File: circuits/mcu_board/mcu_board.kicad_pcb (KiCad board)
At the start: 2 copper layers, 96.3 x 63.9 mm, 44 parts, among them J1 USB_B_Micro, J2 Conn_01x13_Pin, J3 Conn_01x03_Pin, SW1 SW_Push, SW10 SW_Push, SW11 SW_Push, SW12 SW_Push, SW13 SW_Push, SW2 SW_Push, SW3 SW_Push, SW4 SW_Push, SW5 SW_Push, SW6 SW_Push, SW7 SW_Push, SW8 SW_Push, SW9 SW_Push, U1 AMS1117-3.3, U4 STM32F302CCTx, Y1 8MHz

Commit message: 修改单片机型号
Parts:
- U4: value STM32F302CCTx -> STM32F103CBTx

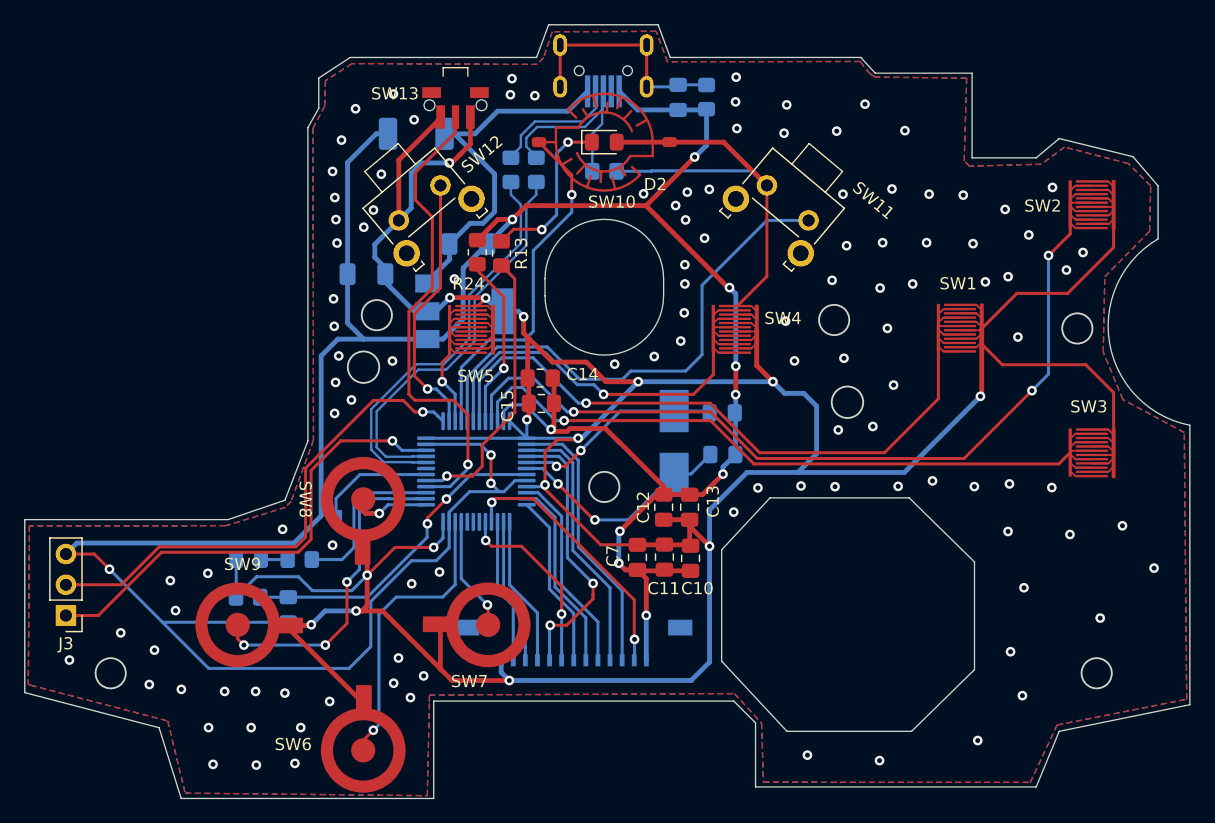
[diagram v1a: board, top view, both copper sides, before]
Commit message: 手柄板更新按键封装
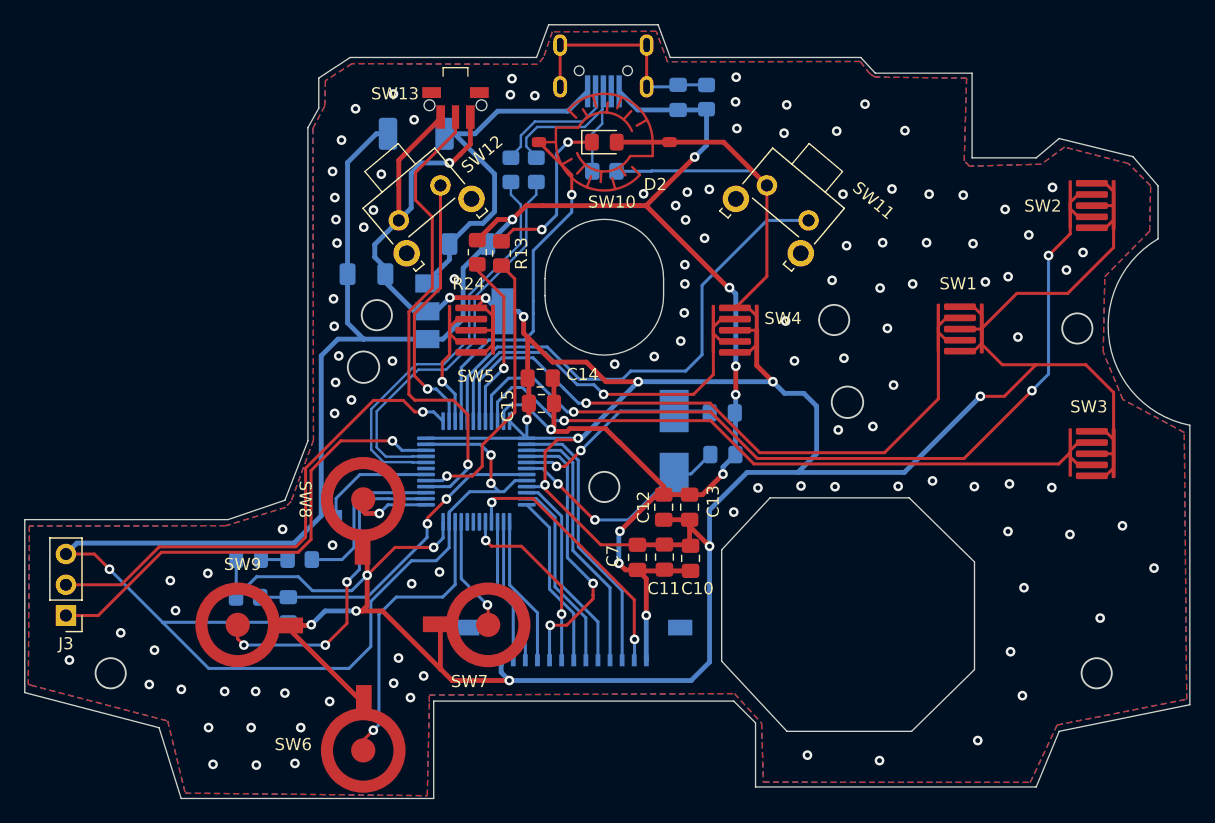
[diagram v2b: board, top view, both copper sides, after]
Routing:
- net +3V3: track 424.4 -> 407.6 mm
- net /BTN_A: track 68.1 -> 61.1 mm
- net /BTN_X: track 68.7 -> 61.7 mm
- net /BTN_Y: track 84.9 -> 77.9 mm
- net /BTN_RM: track 45.9 -> 38.9 mm
- net /BTN_LM: track 24.1 -> 17.1 mm

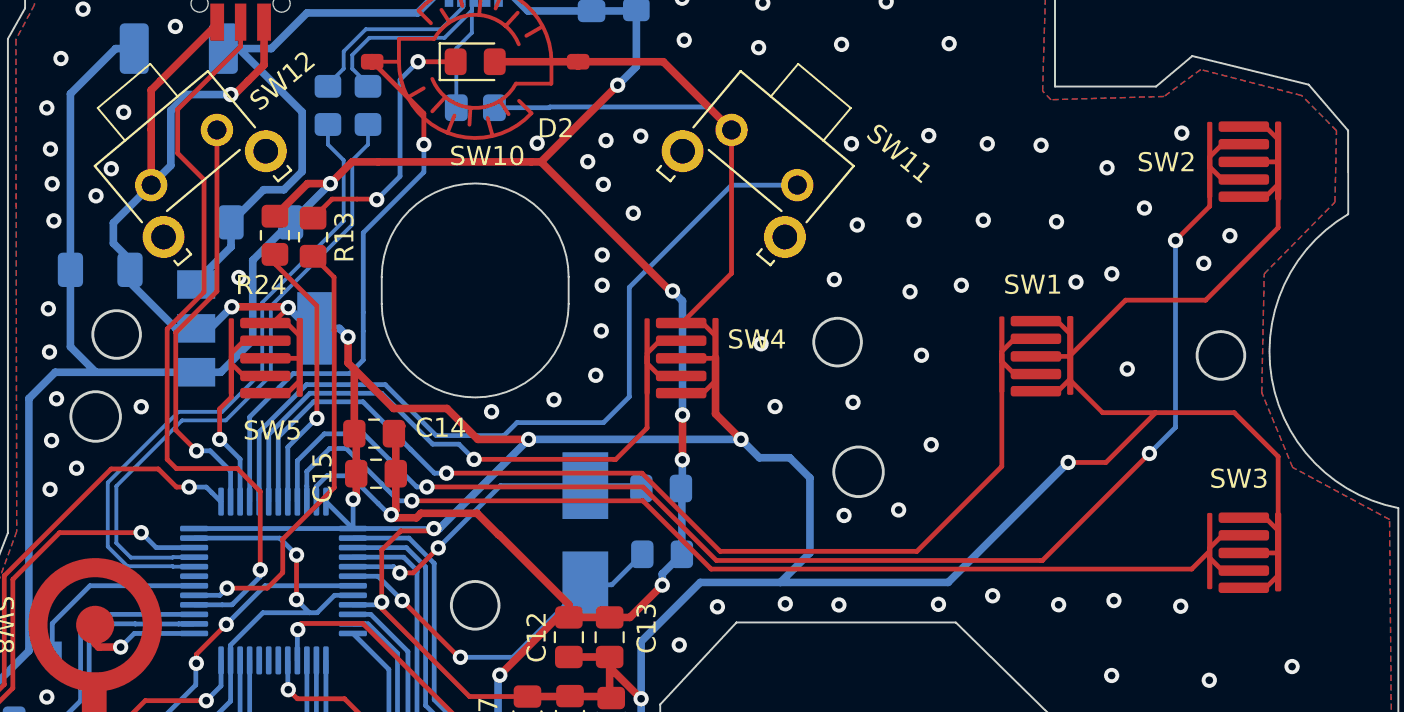
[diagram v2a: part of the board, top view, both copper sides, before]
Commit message: mcu板更新封装
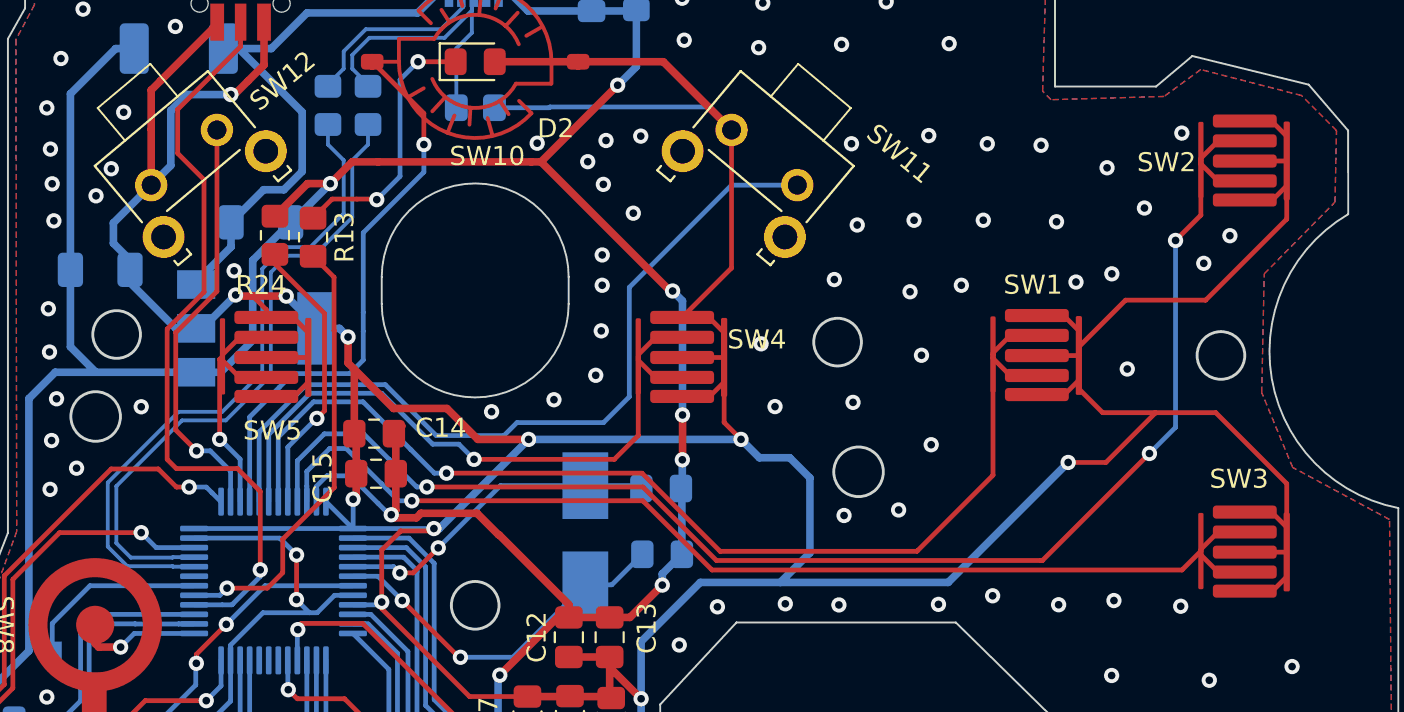
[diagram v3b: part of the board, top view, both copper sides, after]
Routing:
- net +3V3: track 407.6 -> 400.2 mm
- net /BTN_A: track 61.1 -> 57.7 mm
- net /BTN_LM: track 17.1 -> 13.8 mm
- net /BTN_X: track 61.7 -> 58.5 mm
- net /BTN_Y: track 77.9 -> 74.6 mm
- net /BTN_RM: track 38.9 -> 37.8 mm
- net /MCU_D+: track 33.2 -> 34.0 mm
- net /MCU_D-: track 33.9 -> 34.7 mm

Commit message: 更新按键封装
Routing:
- net +3V3: track 400.2 -> 395.9 mm
- net /BTN_A: track 57.7 -> 61.8 mm
- net /BTN_Y: track 74.6 -> 75.8 mm
- net /BTN_X: track 58.5 -> 59.5 mm
- net /BTN_RM: track 37.8 -> 38.8 mm
- net /BTN_LM: track 13.8 -> 14.8 mm

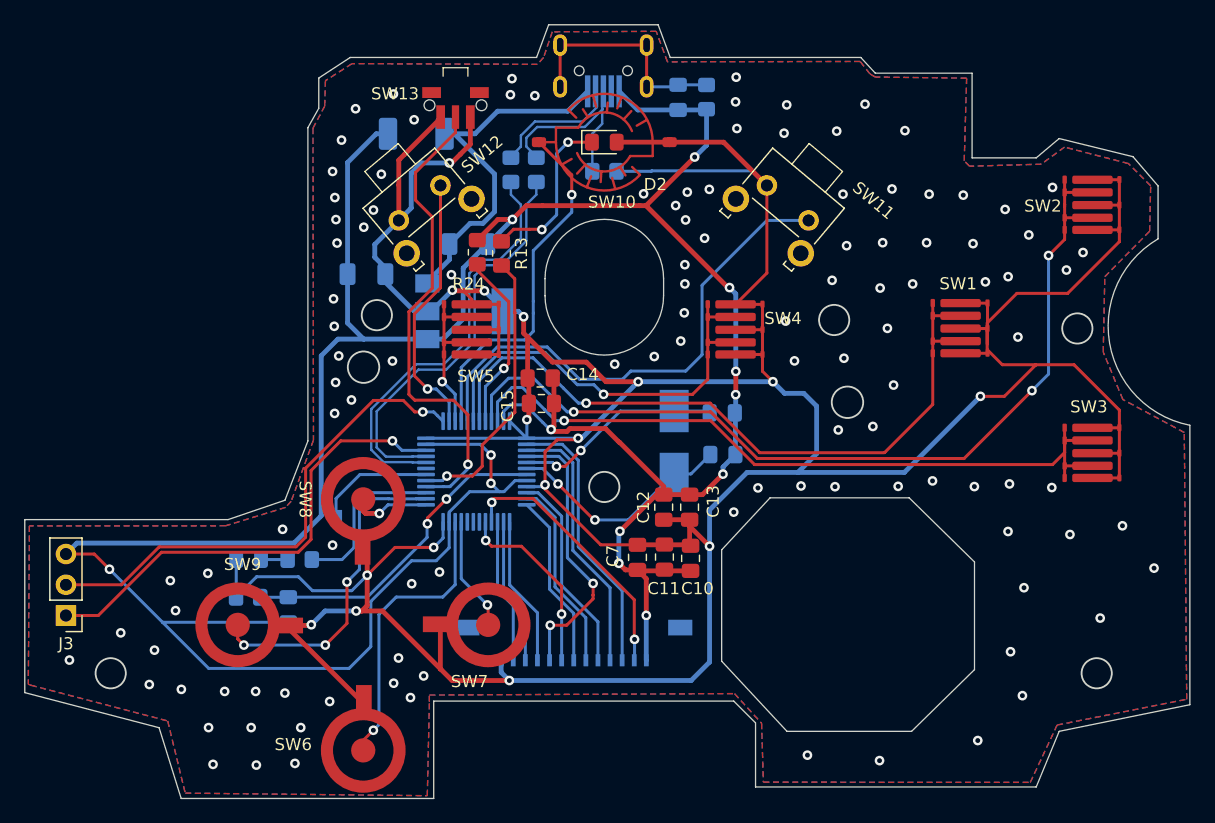
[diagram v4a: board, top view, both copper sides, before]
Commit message: 差手柄机械按键位置
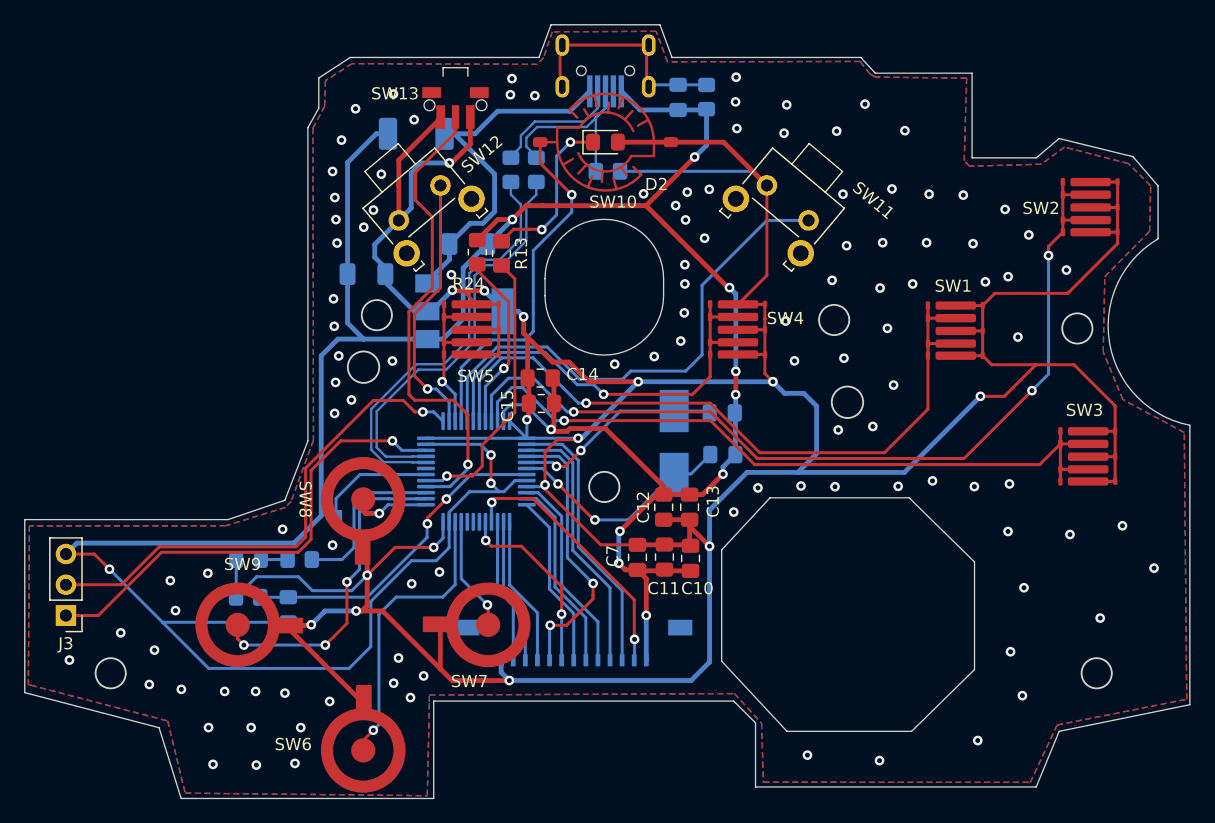
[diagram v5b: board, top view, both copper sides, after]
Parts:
- moved SW3 0.45 mm to (200.8, 112.1)
- moved SW1 0.45 mm to (189.9, 101.7)
- moved R10 0.29 mm to (161.1, 88.5)
- moved SW2 0.25 mm to (201.1, 91.5)
- moved SW4 0.20 mm to (171.9, 101.6)
- moved J1 0.18 mm to (160.9, 79.0)
- moved D2 0.10 mm to (160.9, 86.1)
- moved SW10 0.10 mm to (160.9, 86.1)
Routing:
- net +3V3: track 395.9 -> 392.6 mm
- net /BTN_A: track 61.8 -> 60.7 mm
- net GND: track 258.1 -> 257.9 mm, vias 127 -> 124
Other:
- outline, holes or cut-outs redrawn

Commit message: 调整封装,待打样测试
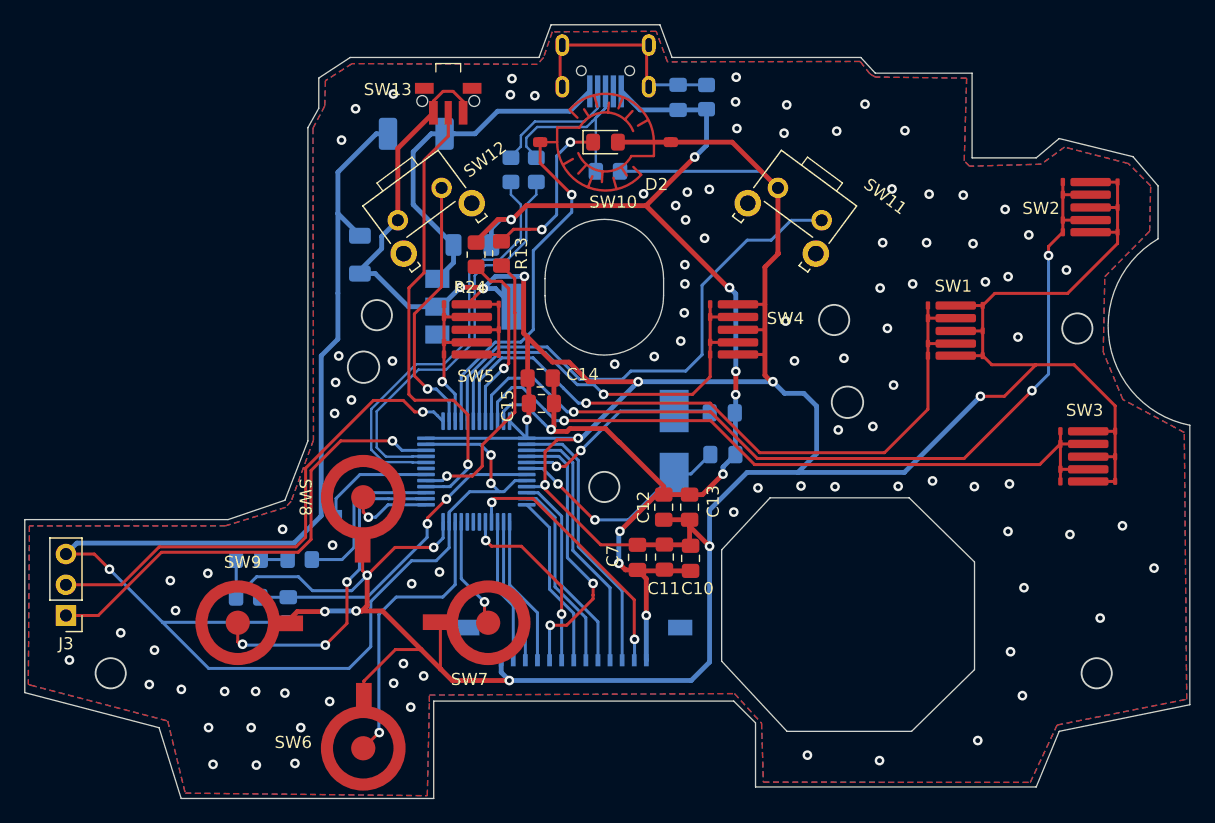
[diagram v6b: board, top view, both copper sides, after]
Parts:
- moved C3 1.70 mm to (140.6, 95.4), turned to 90 degrees
- moved SW11 1.00 mm to (176.9, 91.3), turned to -36.5 degrees
- moved U1 0.91 mm to (150.2, 99.7)
- moved SW13 0.69 mm to (147.9, 82.7)
- moved C2 0.35 mm to (149.9, 94.6)
- moved R24 0.22 mm to (150.2, 95.4)
- moved SW6 0.18 mm to (140.9, 136.2)
- moved SW7 0.17 mm to (151.2, 125.8)
- moved SW8 0.17 mm to (140.9, 115.5)
- moved SW9 0.17 mm to (130.5, 125.8)
- moved SW12 0.10 mm to (145.6, 91.3), turned to 36.5 degrees
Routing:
- net GND: track 257.9 -> 243.2 mm, vias 124 -> 110
- net /BTN_RB: track 42.8 -> 43.9 mm
- net /BTN_PAIR: track 39.8 -> 38.7 mm
- net +3V3: track 392.6 -> 391.6 mm, vias 16 -> 15
- net VBUS: track 30.9 -> 29.9 mm
- net Net-(U4-BOOT0): track 14.8 -> 15.6 mm
- net /BTN_DOWN: track 24.3 -> 25.0 mm
- net /BTN_XBOX: track 29.7 -> 29.2 mm

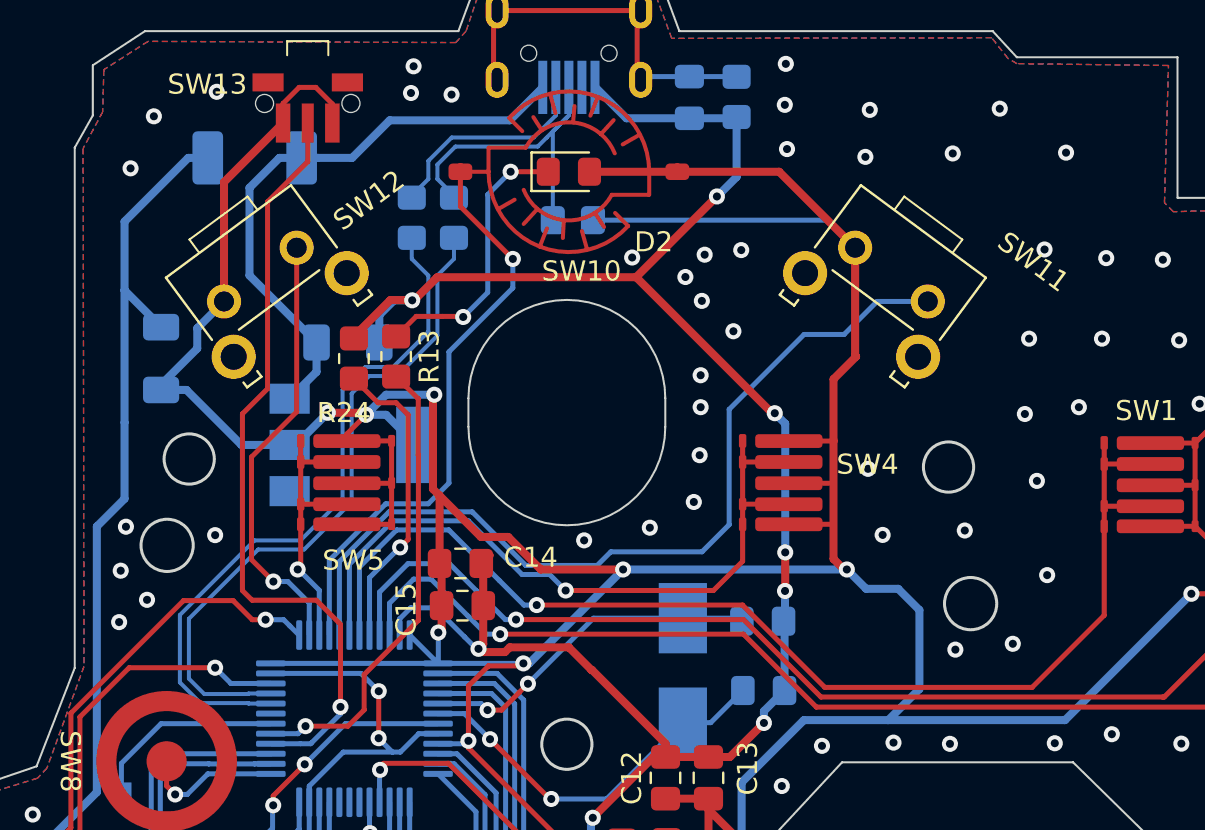
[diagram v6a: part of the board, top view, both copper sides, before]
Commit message: 微调了LB RB位置
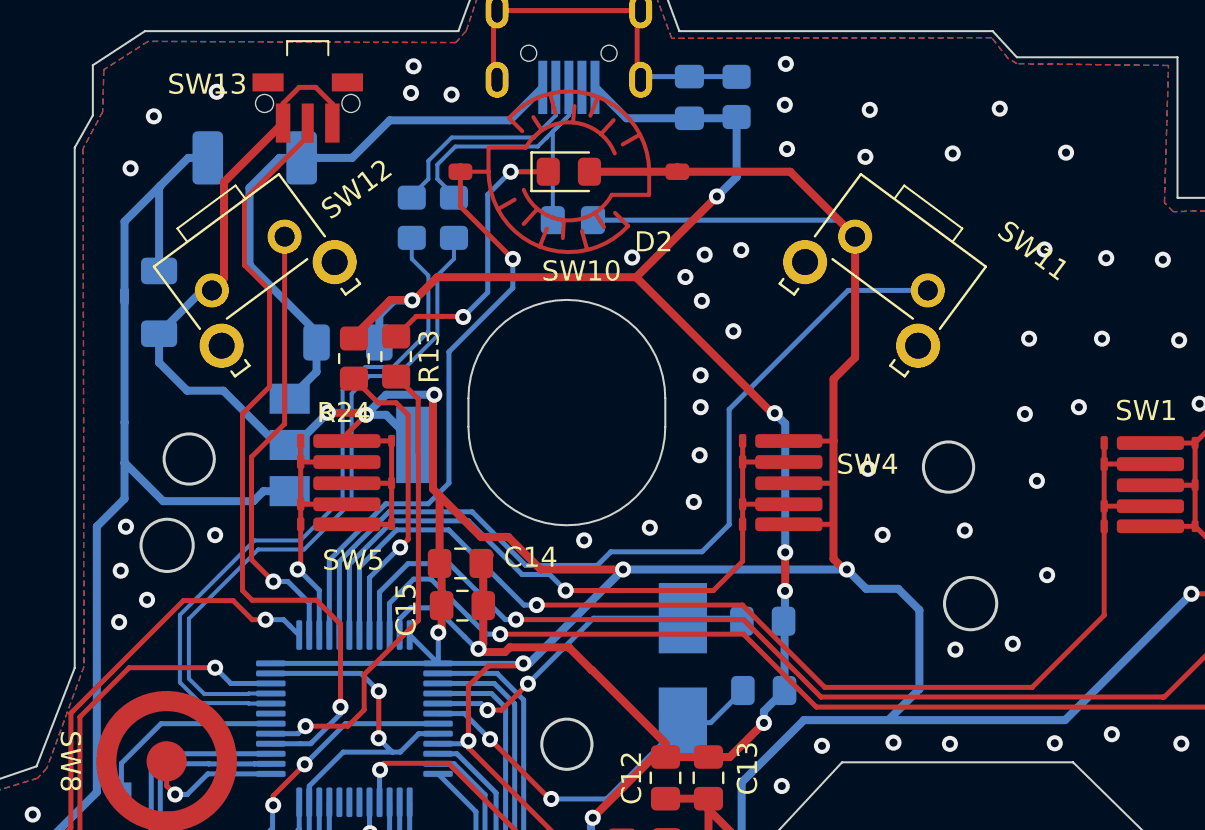
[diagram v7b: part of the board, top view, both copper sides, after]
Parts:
- moved C3 2.80 mm to (140.5, 92.6)
- moved SW12 0.81 mm to (145.0, 90.8)
- moved SW11 0.55 mm to (176.9, 90.8)
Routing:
- net GND: track 243.2 -> 254.7 mm
- net /BTN_PAIR: track 38.7 -> 39.8 mm

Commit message: 微调LB RB
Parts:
- moved SW11 0.75 mm to (176.9, 91.5)
- moved SW12 0.45 mm to (145.0, 91.2)
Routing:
- net +3V3: track 391.3 -> 391.9 mm
